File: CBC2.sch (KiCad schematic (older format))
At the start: 209 parts, among them K0:0 KEYSW, K0:1 KEYSW, K0:10 KEYSW, K0:11 KEYSW, K0:12 KEYSW, K0:13 KEYSW, K0:14 KEYSW, K0:15 KEYSW, K0:2 KEYSW, K0:3 KEYSW, K0:4 KEYSW, K0:5 KEYSW, K0:6 KEYSW, K0:7 KEYSW, K0:8 KEYSW, K0:9 KEYSW, K1:0 KEYSW, K1:1 KEYSW, K1:10 KEYSW, K1:11 KEYSW, K1:12 KEYSW, K1:13 KEYSW, K1:14 KEYSW, K1:15 KEYSW, K1:16 KEYSW, K1:17 KEYSW, K1:18 KEYSW, K1:2 KEYSW, K1:3 KEYSW, K1:4 KEYSW, K1:5 KEYSW, K1:6 KEYSW, K1:7 KEYSW, K1:8 KEYSW, K1:9 KEYSW, K2:0 KEYSW, K2:1 KEYSW, K2:10 KEYSW, K2:11 KEYSW, K2:12 KEYSW, K2:13 KEYSW, K2:14 KEYSW, K2:15 KEYSW, K2:16 KEYSW, K2:17 KEYSW, K2:18 KEYSW, K2:2 KEYSW, K2:3 KEYSW, K2:4 KEYSW, K2:5 KEYSW, K2:6 KEYSW, K2:7 KEYSW, K2:8 KEYSW, K2:9 KEYSW, K3:0 KEYSW, K3:1 KEYSW, K3:10 KEYSW, K3:11 KEYSW, K3:12 KEYSW, K3:14 KEYSW, K3:15 KEYSW, K3:16 KEYSW, K3:17 KEYSW, K3:2 KEYSW, K3:3 KEYSW, K3:4 KEYSW, K3:5 KEYSW, K3:6 KEYSW, K3:7 KEYSW, K3:8 KEYSW, K3:9 KEYSW, K4:0 KEYSW, K4:10 KEYSW, K4:11 KEYSW, K4:12 KEYSW, K4:14 KEYSW, K4:15 KEYSW, K4:16 KEYSW, K4:17 KEYSW, K4:18 KEYSW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

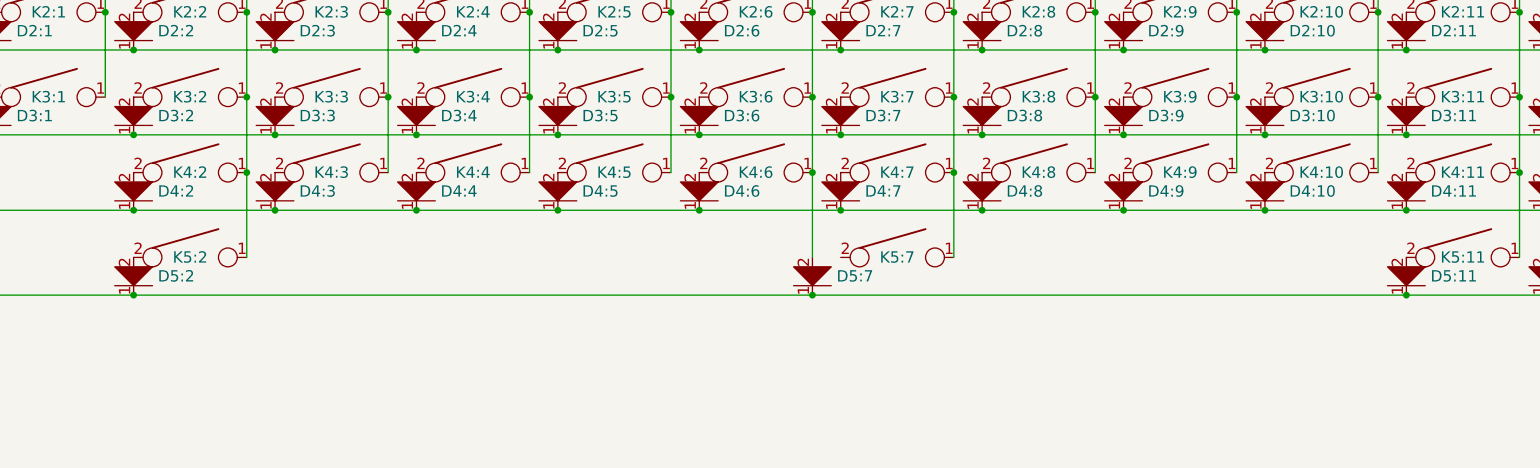
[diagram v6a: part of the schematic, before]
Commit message: updated footprints for layout adjustment. placed diodes, still on the fence about the microcontroller placement
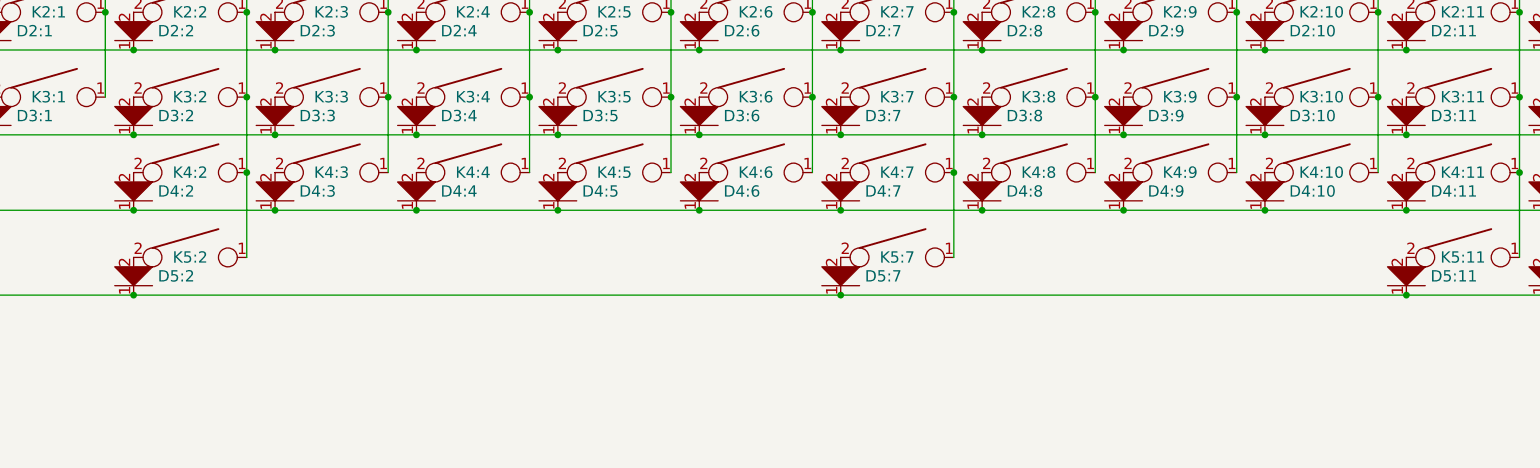
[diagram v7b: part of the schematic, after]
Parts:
- K1:13: footprint MX_Alps_Hybrid:MX-1.75U -> MX_Alps_Hybrid:MX-2U
- K2:13: footprint MX_Alps_Hybrid:MX-1.25U -> MX_Alps_Hybrid:MX-1.5U
- K3:12: footprint MX_Alps_Hybrid:MX-2U -> MX_Alps_Hybrid:MX-2.25U
- K4:12: footprint MX_Alps_Hybrid:MX-2.5U -> MX_Alps_Hybrid:MX-2.75U
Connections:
- net col6: no longer D5:7.2
- net at K5:7.2: now also D5:7.2
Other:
- moved on the sheet: D5:7
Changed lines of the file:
@@
 F 0 "K1:13" H 15400 3200 60  0000 C CNN
 F 1 "KEYSW" H 15400 3100 60  0001 C CNN
-F 2 "MX_Alps_Hybrid:MX-1.75U" H 15400 3200 60  0001 C CNN
+F 2 "MX_Alps_Hybrid:MX-2U" H 15400 3200 60  0001 C CNN
 F 3 "" H 15400 3200 60  0000 C CNN
 	1    15400 3200
@@
 F 0 "K3:12" H 14650 4100 60  0000 C CNN
 F 1 "KEYSW" H 14650 4000 60  0001 C CNN
-F 2 "MX_Alps_Hybrid:MX-2U" H 14650 4100 60  0001 C CNN
+F 2 "MX_Alps_Hybrid:MX-2.25U" H 14650 4100 60  0001 C CNN
 F 3 "" H 14650 4100 60  0000 C CNN
 	1    14650 4100
@@
 L CBC2-rescue:D-keyboard_parts-CBC2-rescue D5:7
 U 1 1 5CBDF3DD
-P 10450 5100
-F 0 "D5:7" H 10322 5050 60  0000 R CNN
-F 1 "D" V 10600 5050 60  0001 C CNN
-F 2 "Keebio-Parts:Diode-dual" H 10450 5100 60  0001 C CNN
-F 3 "" H 10450 5100 60  0000 C CNN
-	1    10450 5100
+P 10600 5100
+F 0 "D5:7" H 10472 5050 60  0000 R CNN
+F 1 "D" V 10750 5050 60  0001 C CNN
+F 2 "Keebio-Parts:Diode-dual" H 10600 5100 60  0001 C CNN
+F 3 "" H 10600 5100 60  0000 C CNN
+	1    10600 5100
 	-1   0    0    1
 $EndComp
@@
 F 0 "K2:13" H 15400 3650 60  0000 C CNN
 F 1 "KEYSW" H 15400 3550 60  0001 C CNN
-F 2 "MX_Alps_Hybrid:MX-1.25U" H 15400 3650 60  0001 C CNN
+F 2 "MX_Alps_Hybrid:MX-1.5U" H 15400 3650 60  0001 C CNN
 F 3 "" H 15400 3650 60  0000 C CNN
 	1    15400 3650
@@
 F 0 "K4:12" H 14650 4500 60  0000 C CNN
 F 1 "KEYSW" H 14650 4400 60  0001 C CNN
-F 2 "MX_Alps_Hybrid:MX-2.5U" H 14650 4500 60  0001 C CNN
+F 2 "MX_Alps_Hybrid:MX-2.75U" H 14650 4500 60  0001 C CNN
 F 3 "" H 14650 4500 60  0000 C CNN
 	1    14650 4500
@@
 Wire Wire Line
 	5350 4700 6850 4700
-Wire Wire Line
-	10450 4500 10450 4950
-Connection ~ 10450 4500
 Connection ~ 14350 5150
 Wire Wire Line
@@
 	14200 4500 14200 4950
 Connection ~ 14200 4500
-Connection ~ 10450 5150
-Wire Wire Line
-	10450 5150 13600 5150
 Wire Wire Line
 	11200 4500 11200 4950
@@
 Connection ~ 6850 5150
 Wire Wire Line
-	6850 5150 10450 5150
-Wire Wire Line
 	5350 5150 6850 5150
 Wire Wire Line
 	7450 4500 7450 4950
 Connection ~ 7450 4500
+Connection ~ 10600 5150
+Wire Wire Line
+	10600 5150 13600 5150
+Wire Wire Line
+	6850 5150 10600 5150
 $EndSCHEMATC
